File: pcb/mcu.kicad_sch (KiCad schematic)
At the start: 42 parts, among them J2 Fermion 1.8" TFT LCD, J4 Potentiometer, J4 UART, J7 SWD, SW1 SW_Push, SW2 SW_Push, U1 STM32F411CEU6, Y1 25MHz 9pF

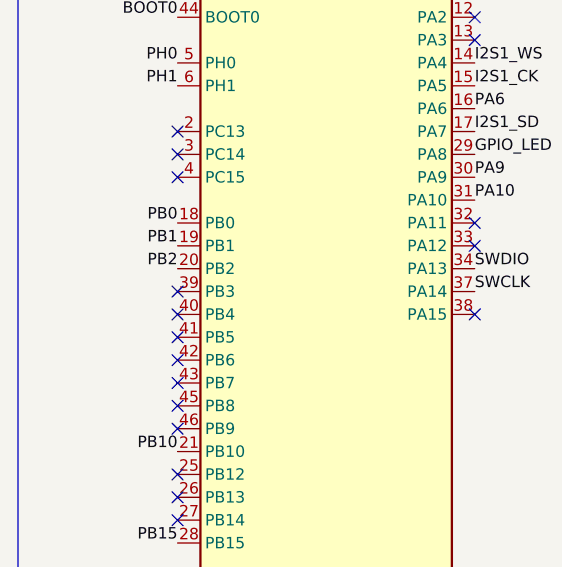
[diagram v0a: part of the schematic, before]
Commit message: Connected SWO pin
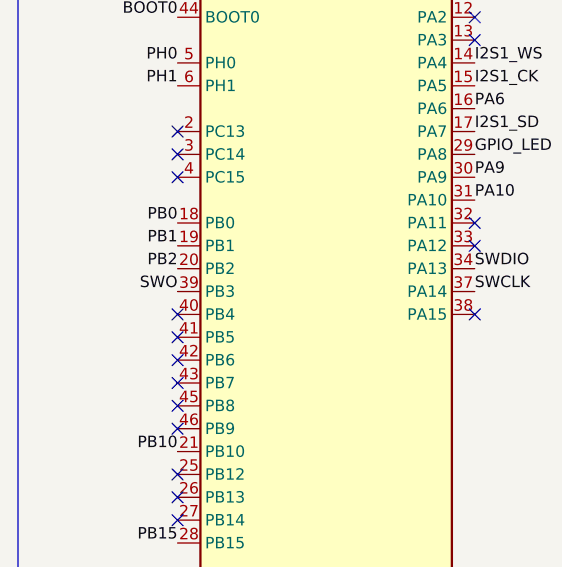
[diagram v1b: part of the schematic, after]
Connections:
- net SWO: now also U1.39 (PB3)
- no-connect marks 20 -> 19
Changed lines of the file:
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@@
   (no_connect (at 34.7726 89.8144))
   (no_connect (at 34.7726 49.1744))
-  (no_connect (at 34.7726 66.9544))
   (no_connect (at 34.7726 54.2544))
   (no_connect (at 34.7726 72.0344))
@@
     (effects (font (size 1.27 1.27)) (justify right bottom))
   )
+  (label "SWO" (at 34.7726 66.9544 180) (fields_autoplaced)
+    (effects (font (size 1.27 1.27)) (justify right bottom))
+  )

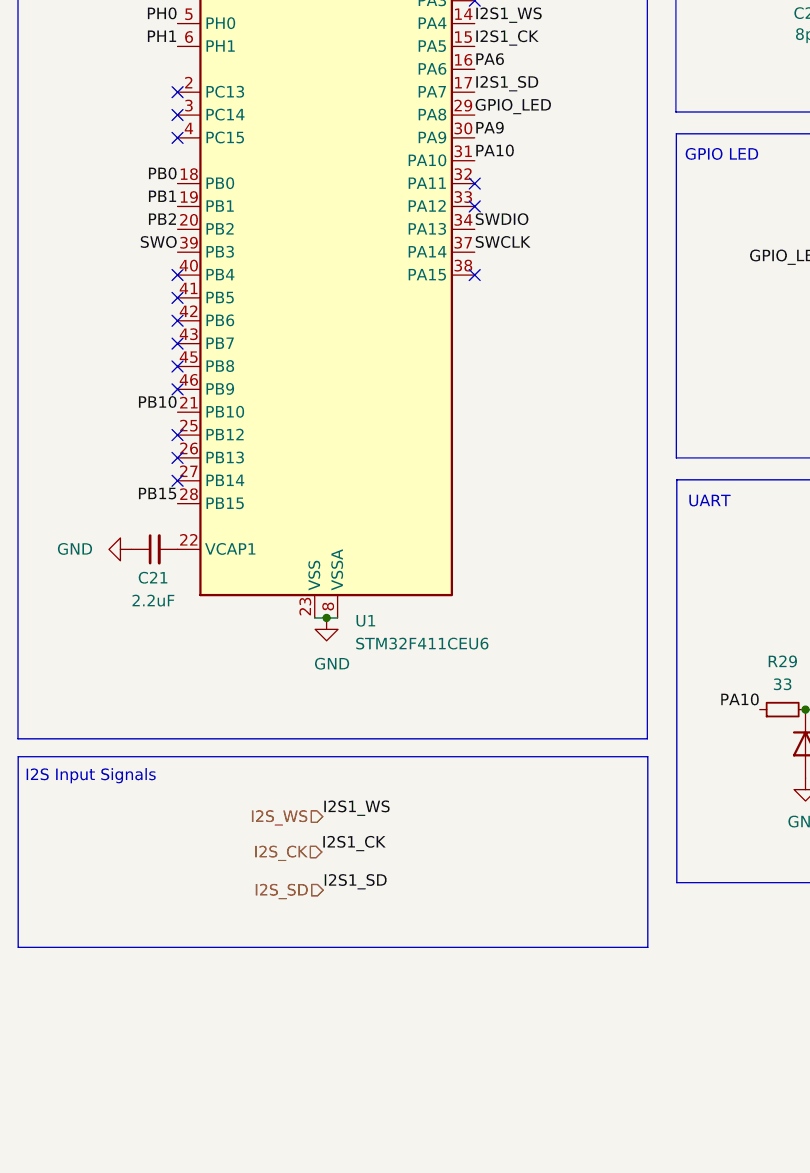
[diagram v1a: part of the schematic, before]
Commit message: Added input GPIO to check muted state
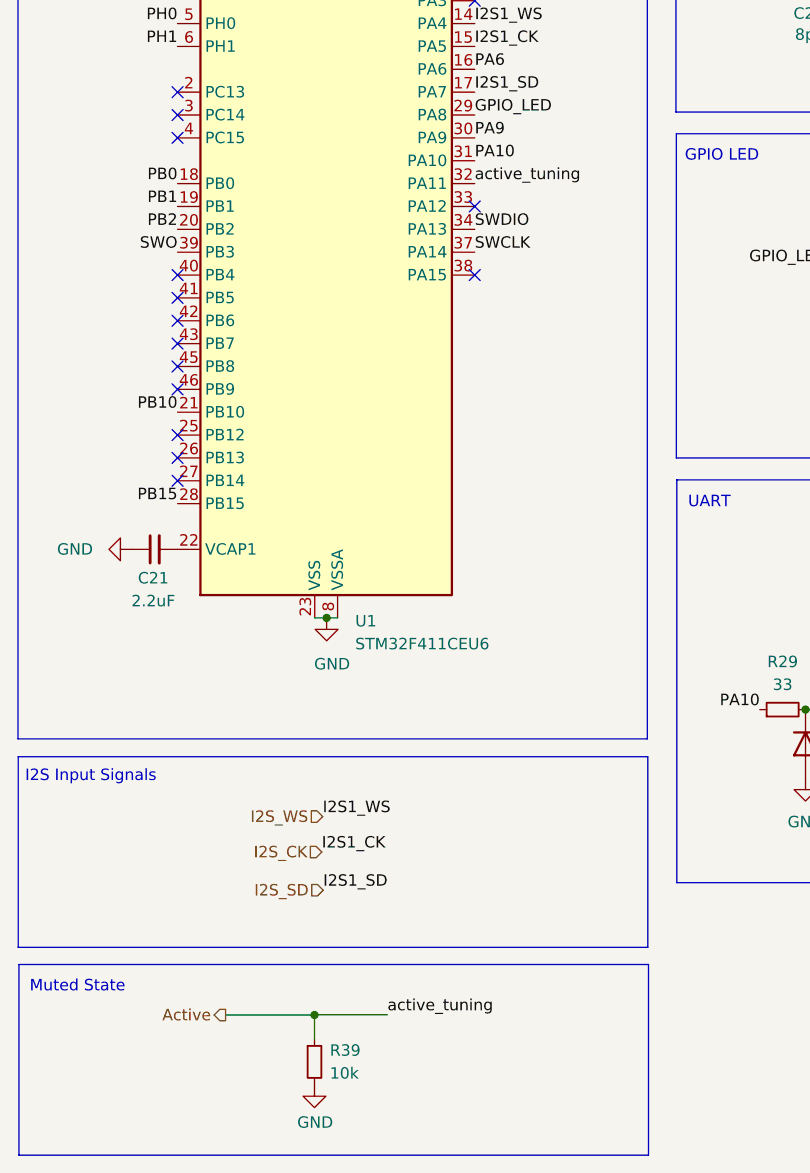
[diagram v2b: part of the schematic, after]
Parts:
- added R39: 10k, symbol Device:R_Small
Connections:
- net GND: now also R39.2
- net Active: now reaches U1.32 (PA11)
- net Active: now also R39.1
- no-connect marks 19 -> 18
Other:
- note added: "Muted State"
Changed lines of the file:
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@@
   (junction (at 211.7598 78.0796) (diameter 0) (color 0 0 0 0)
+  )
+  (junction (at 49.9872 151.7142) (diameter 0) (color 0 0 0 0)
   )
   (junction (at 158.9024 71.3486) (diameter 0) (color 0 0 0 0)
@@
   (no_connect (at 67.7926 61.8744))
   (no_connect (at 34.7726 51.7144))
-  (no_connect (at 67.7926 59.3344))
   (no_connect (at 34.7726 89.8144))
   (no_connect (at 34.7726 49.1744))
@@
     (stroke (width 0) (type default))
   )
+  (wire (pts (xy 49.9872 151.7142) (xy 49.9872 154.3812))
+    (stroke (width 0) (type default))
+  )
   (wire (pts (xy 113.9698 37.228) (xy 128.143 37.228))
     (stroke (width 0) (type default))
@@
     (stroke (width 0) (type default))
   )
+  (wire (pts (xy 49.9872 151.7142) (xy 49.9872 151.6888))
+    (stroke (width 0) (type default))
+  )
   (wire (pts (xy 113.9698 37.228) (xy 113.9698 34.2392))
     (stroke (width 0) (type default))
@@
     (stroke (width 0) (type default))
   )
+  (wire (pts (xy 40.1066 151.7142) (xy 49.9872 151.7142))
+    (stroke (width 0) (type default))
+  )
   (wire (pts (xy 169.1132 74.549) (xy 169.1132 71.3486))
     (stroke (width 0) (type default))
@@
     (stroke (width 0) (type default))
   )
+  (wire (pts (xy 58.0898 151.6888) (xy 49.9872 151.6888))
+    (stroke (width 0) (type default))
+  )
   (wire (pts (xy 172.0596 35.433) (xy 161.6964 35.433))
     (stroke (width 0) (type default))
@@
     (fill (type none))
   )
+  (rectangle (start 17.145 146.1008) (end 87.0966 167.2844)
+    (stroke (width 0) (type default))
+    (fill (type none))
+  )
   (rectangle (start 184.277 53.6956) (end 223.3422 89.7128)
     (stroke (width 0) (type default))
@@
     (effects (font (size 1.27 1.27)) (justify left bottom))
   )
+  (text "Muted State" (at 18.3388 149.3774 0)
+    (effects (font (size 1.27 1.27)) (justify left bottom))
+  )
   (text "NRST" (at 144.272 56.896 0)
     (effects (font (size 1.27 1.27)) (justify left bottom))
@@
     (effects (font (size 1.27 1.27)) (justify left bottom))
   )
+  (label "active_tuning" (at 67.7926 59.3344 0) (fields_autoplaced)
+    (effects (font (size 1.27 1.27)) (justify left bottom))
+  )
   (label "SWDIO" (at 67.7926 64.4144 0) (fields_autoplaced)
     (effects (font (size 1.27 1.27)) (justify left bottom))
@@
     (effects (font (size 1.27 1.27)) (justify right bottom))
   )
+  (label "active_tuning" (at 58.0898 151.6888 0) (fields_autoplaced)
+    (effects (font (size 1.27 1.27)) (justify left bottom))
+  )
   (label "I2S1_SD" (at 50.9524 137.8458 0) (fields_autoplaced)
     (effects (font (size 1.27 1.27)) (justify left bottom))
@@
   (label "SWDIO" (at 244.7036 66.1162 180) (fields_autoplaced)
     (effects (font (size 1.27 1.27)) (justify right bottom))
+  )
+  (hierarchical_label "Active" (shape output) (at 40.1066 151.7142 180) (fields_autoplaced)
+    (effects (font (size 1.27 1.27)) (justify right))
   )
   (hierarchical_label "I2S_SD" (shape input) (at 50.9524 137.8458 180) (fields_autoplaced)
@@
     )
   )
+  (symbol (lib_id "Device:R_Small") (at 49.9872 156.9212 0) (unit 1)
+    (in_bom yes) (on_board yes) (dnp no) (fields_autoplaced)
+    (property "Reference" "R39" (at 51.689 155.6512 0)
+      (effects (font (size 1.27 1.27)) (justify left))
+    )
+    (property "Value" "10k" (at 51.689 158.1912 0)
+      (effects (font (size 1.27 1.27)) (justify left))
+    )
+    (property "Footprint" "" (at 49.9872 156.9212 0)
+      (effects (font (size 1.27 1.27)) hide)
+    )
+    (property "Datasheet" "~" (at 49.9872 156.9212 0)
+      (effects (font (size 1.27 1.27)) hide)
+    )
+    (pin "1")
+    (pin "2")
+    (instances
+      (project "tuner_pedal"
+        (path "/be09f3cc-c79c-49de-93a4-4a01bf6bfbcf/23f7357b-d90b-4d34-9d76-13515b2796f4"
+          (reference "R39") (unit 1)
+        )
+      )
+    )
+  )
   (symbol (lib_id "power:+3.3V") (at 161.6964 30.353 0) (unit 1)
     (in_bom yes) (on_board yes) (dnp no)
@@
         )
       )
+    )
+  )
+  (symbol (lib_id "power:GND") (at 49.9872 159.4612 0) (unit 1)
+    (in_bom yes) (on_board yes) (dnp no)
+    (property "Reference" "#PWR079" (at 49.9872 165.8112 0)
+      (effects (font (size 1.27 1.27)) hide)
+    )
+    (property "Value" "GND" (at 50.0634 163.6522 0)
+      (effects (font (size 1.27 1.27)))
+    )
+    (property "Footprint" "" (at 49.9872 159.4612 0)
+      (effects (font (size 1.27 1.27)) hide)
+    )
+    (property "Datasheet" "" (at 49.9872 159.4612 0)
+      (effects (font (size 1.27 1.27)) hide)
+    )
+    (pin "1")
+    (instances
+      (project "tuner_pedal"
+        (path "/be09f3cc-c79c-49de-93a4-4a01bf6bfbcf/23f7357b-d90b-4d34-9d76-13515b2796f4"
+          (reference "#PWR079") (unit 1)
+        )
+      )
